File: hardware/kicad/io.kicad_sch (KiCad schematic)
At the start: 46 parts, among them J5 JST-XH 4p, J6 JST-XH 4p, J7 JST-XH 3p, J8 JST-XH 4p, J9 JST-XH 5p

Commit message: Add routed controller PCB, clutch CAD and mill notes
- Schematic: panel ribbon (2x7 IDC) + feed-unit header (JST-XH 7) so all
  connectors fit one 100 mm board edge; fix stub-bridging in the generator.
- PCB (hardware/tools/build_pcb.py): 100x100 mm 4-layer board built from the
  netlist - fixed placement for power/connectors, auto-placed passives,
  GND / split +36V/+3V3 inner planes, Freerouting, post-route power pours,
  GND stitching; fix_planes.py drops plane vias for leftovers;
  check_pcb.py runs DRC with schematic parity. 3D renders in hardware/renders.
  Status: 5 unconnected items + 2 starved thermals left for interactive
  routing (see hardware/kicad/drc.json after check_pcb.py).
- mechanical/clutch: parametric build123d model of the DIY tooth clutch
  (field housing, coil, rotor, armature, leaf springs, output hub/shaft,
  cover), STEP/STL export and VTK renders.
- docs/mill.md: SIEG X3.5D research and the measurements still needed.

Co-Authored-By: Claude Opus 5.5 <noreply@anthropic.com>
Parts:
- removed J6, J8: JST-XH 4p, Connector_JST:JST_XH_B4B-XH-A_1x04_P2.50mm_Vertical, symbol Connector_Generic:Conn_01x04
- removed J7: JST-XH 3p, Connector_JST:JST_XH_B3B-XH-A_1x03_P2.50mm_Vertical, symbol Connector_Generic:Conn_01x03
- removed J9: JST-XH 5p, Connector_JST:JST_XH_B5B-XH-A_1x05_P2.50mm_Vertical, symbol Connector_Generic:Conn_01x05
- added J4: PANEL 2x7 IDC, Connector_IDC:IDC-Header_2x07_P2.54mm_Vertical, symbol Connector_Generic:Conn_02x07_Odd_Even
- J5: value JST-XH 4p -> JST-XH 7p; footprint Connector_JST:JST_XH_B4B-XH-A_1x04_P2.50mm_Vertical -> Connector_JST:JST_XH_B7B-XH-A_1x07_P2.50mm_Vertical; symbol Connector_Generic:Conn_01x04 -> Connector_Generic:Conn_01x07; LCSC C144395 -> (none); MPN JST B4B-XH-A(LF)(SN) -> JST B7B-XH-A(LF)(SN)
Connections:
- net +3V3: now also J4.2 (Pin_2)
- net +5V: now also J5.1 (Pin_1)
- net DIAL_A_RAW: now also J4.11 (Pin_11)
- net DIAL_B_RAW: now also J4.12 (Pin_12)
- net DIAL_SW_RAW: now also J4.13 (Pin_13)
- net ENC_A_RAW: now also J5.3 (Pin_3)
- net ENC_B_RAW: now also J5.4 (Pin_4)
- net ENC_N_RAW: now also J5.5 (Pin_5)
- net ESTOP_RET: now also J4.7 (Pin_7)
- net GND: now also J5.2 (Pin_2), J4.1 (Pin_1), J4.14 (Pin_14), J4.5 (Pin_5); no longer J5.1 (Pin_1)
- net LIM_L_RAW: now also J5.6 (Pin_6)
- net LIM_R_RAW: now also J5.7 (Pin_7)
- net MODE_L_RAW: now also J4.8 (Pin_8); no longer J5.2 (Pin_2)
- net MODE_R_RAW: now also J4.9 (Pin_9); no longer J5.3 (Pin_3)
- net OLED_SCL: now also J4.3 (Pin_3)
- net OLED_SDA: now also J4.4 (Pin_4)
- net RAPID_RAW: now also J4.10 (Pin_10); no longer J5.4 (Pin_4)
- new net ESTOP_SRC: J4.6 (Pin_6)
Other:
- moved on the sheet: C36, C37, C38, C39, C40, C41, C42, C43, C44, C45, C46, D10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

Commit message: Complete LCSC part numbers in the BOM
Every BOM line now has an LCSC number except the Pico module (A1), which
is marked "user-supplied, hand-solder". Parts were checked against the
JLCPCB parts library for spec, Basic/Extended status and stock.

- build_schematic.py: RES_PARTS / CAP_PARTS value+footprint lookup tables
  used by R() / C(), which now raise if a passive has no entry; props for
  the diodes, LEDs, logic ICs, PTC (Littelfuse 2920L050DR, 60 V), IDC
  header (ZHOURI DC3-2.54-14PAS), JST-XH 7p and the Omron B3S-1000 reset
  button.
- Regenerated the schematic sheets, kicad/bom.csv, fab BOM and the README
  missing-LCSC table. PCB, CPL, gerbers and drills are unchanged.

Co-Authored-By: Claude Sonnet 5.5 <noreply@anthropic.com>
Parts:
- C36, C37, C38, C43: LCSC (none) -> C14663; MPN (none) -> Yageo CC0603KRX7R9BB104
- C39, C40, C41, C42: LCSC (none) -> C57112; MPN (none) -> FH 0603B103K500NT
- C44, C45, C46: LCSC (none) -> C14858; MPN (none) -> Samsung CL10C101JB8NNNC
- J4: LCSC (none) -> C2977595; MPN 2x7 2.54 mm shrouded box header -> ZHOURI DC3-2.54-14PAS (2x7 shrouded box header)
- J5: LCSC (none) -> C144398
- R48, R50, R52, R54, R56, R58, R60, R62, R70, R71: LCSC (none) -> C25804; MPN (none) -> UNI-ROYAL 0603WAF1002T5E
- R49, R51, R53, R55, R57, R59, R61, R63: LCSC (none) -> C21190; MPN (none) -> UNI-ROYAL 0603WAF1001T5E
- R64, R66, R68: LCSC (none) -> C4190; MPN (none) -> UNI-ROYAL 0603WAF2201T5E
- R65, R67, R69, R72, R73: LCSC (none) -> C22775; MPN (none) -> UNI-ROYAL 0603WAF1000T5E

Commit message: Schematic: bare RP2040 instead of the Pico module
RP2040 (QFN-56) per Raspberry Pi's minimal design: W25Q16JV 2 MB QSPI flash, 12 MHz crystal with 1k series,
internal 1.1 V core regulator, BOOTSEL + RESET buttons, JST-SH SWD, status LED on GPIO25, USB-C (5.1k CC,
27R series). +3V3 now from an AP2112K-3.3 fed by VSYS = +5V or USB VBUS through Schottkys. Same GPIO
numbers as the Pico, so the firmware is unchanged. ERC 0 findings, netlist 132 nets / 189 parts match.
Layout follows (PCB agent). LCSC numbers for the flash and crystal still to be verified.

Co-Authored-By: Claude Opus 5.5 <noreply@anthropic.com>
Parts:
- removed C36, C37, C38, C43: 100nF, Capacitor_SMD:C_0603_1608Metric, symbol Device:C
- removed C39, C40, C41, C42: 10nF, Capacitor_SMD:C_0603_1608Metric, symbol Device:C
- removed C44, C45, C46: 100pF, Capacitor_SMD:C_0603_1608Metric, symbol Device:C
- removed D10, D9: USBLC6-4SC6, Package_TO_SOT_SMD:SOT-23-6, symbol Power_Protection:USBLC6-4SC6
- removed J4: PANEL 2x7 IDC, Connector_IDC:IDC-Header_2x07_P2.54mm_Vertical, symbol Connector_Generic:Conn_02x07_Odd_Even
- removed J5: JST-XH 7p, Connector_JST:JST_XH_B7B-XH-A_1x07_P2.50mm_Vertical, symbol Connector_Generic:Conn_01x07
- removed R48, R50, R52, R54, R56: 10k, Resistor_SMD:R_0603_1608Metric, symbol Device:R
- removed R49, R51, R53, R55: 1k, Resistor_SMD:R_0603_1608Metric, symbol Device:R
- added C53, C54, C55, C60: 100nF, Capacitor_SMD:C_0603_1608Metric, symbol Device:C
- added C56, C57, C58, C59: 10nF, Capacitor_SMD:C_0603_1608Metric, symbol Device:C
- added C61, C62, C63: 100pF, Capacitor_SMD:C_0603_1608Metric, symbol Device:C
- added D13, D14: USBLC6-4SC6, Package_TO_SOT_SMD:SOT-23-6, symbol Power_Protection:USBLC6-4SC6
- added J6: PANEL 2x7 IDC, Connector_IDC:IDC-Header_2x07_P2.54mm_Vertical, symbol Connector_Generic:Conn_02x07_Odd_Even
- added J7: JST-XH 7p, Connector_JST:JST_XH_B7B-XH-A_1x07_P2.50mm_Vertical, symbol Connector_Generic:Conn_01x07
- added R74, R76, R78, R81, R82: 100, Resistor_SMD:R_0603_1608Metric, symbol Device:R
- added R75, R77: 2.2k, Resistor_SMD:R_0603_1608Metric, symbol Device:R
- added R79, R80: 10k, Resistor_SMD:R_0603_1608Metric, symbol Device:R
- R57, R59, R61, R63: value 1k -> 10k; LCSC C21190 -> C25804; MPN UNI-ROYAL 0603WAF1001T5E -> UNI-ROYAL 0603WAF1002T5E
- R58, R60, R62, R70: value 10k -> 1k; LCSC C25804 -> C21190; MPN UNI-ROYAL 0603WAF1002T5E -> UNI-ROYAL 0603WAF1001T5E
- R64, R66, R68: value 2.2k -> 1k; LCSC C4190 -> C21190; MPN UNI-ROYAL 0603WAF2201T5E -> UNI-ROYAL 0603WAF1001T5E
- R65, R67, R69: value 100 -> 10k; LCSC C22775 -> C25804; MPN UNI-ROYAL 0603WAF1000T5E -> UNI-ROYAL 0603WAF1002T5E
- R72: value 100 -> 1k; LCSC C22775 -> C21190; MPN UNI-ROYAL 0603WAF1000T5E -> UNI-ROYAL 0603WAF1001T5E
- R73: value 100 -> 2.2k; LCSC C22775 -> C4190; MPN UNI-ROYAL 0603WAF1000T5E -> UNI-ROYAL 0603WAF2201T5E
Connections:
- net +3V3: now also R57.1, R59.1, R61.1, R63.1, R65.1, R67.1, R69.1, R73.1, D13.5 (VBUS), D14.5 (VBUS), J6.2 (Pin_2), R75.1, R77.1, R79.1, R80.1; no longer R58.1, R60.1, R62.1, R64.1, R66.1, R68.1, R70.1
- net +5V: now also J7.1 (Pin_1)
- net DIAL_A: now also R68.2, C58.1; no longer R59.2
- net DIAL_A_RAW: now also D12.3 (I/O2), R67.2, R68.1, J6.11 (Pin_11); no longer R58.2, R59.1
- net DIAL_B: now also R70.2, C59.1; no longer R61.2
- net DIAL_B_RAW: now also D12.4 (I/O3), R69.2, R70.1, J6.12 (Pin_12); no longer R60.2, R61.1
- net DIAL_SW: now also R72.2, C60.1; no longer R63.2
- net DIAL_SW_RAW: now also D12.6 (I/O4), R71.2, R72.1, J6.13 (Pin_13); no longer R62.2, R63.1
- net ENC_A_RAW: now also R73.2, D13.1 (I/O1), J7.3 (Pin_3), R74.1; no longer D11.1 (I/O1), R64.2, R65.1
- net ENC_B_RAW: now also D13.3 (I/O2), J7.4 (Pin_4), R75.2, R76.1; no longer D11.3 (I/O2), R66.2, R67.1
- net ENC_N_RAW: now also D13.4 (I/O3), J7.5 (Pin_5), R77.2, R78.1; no longer D11.4 (I/O3), R68.2, R69.1
- net ENC_OUT_A: now also C61.1, R74.2; no longer R65.2
- net ENC_OUT_B: now also C62.1, R76.2; no longer R67.2
- net ENC_OUT_N: now also C63.1, R78.2; no longer R69.2
- net ESTOP_RET: now also D13.6 (I/O4), J6.7 (Pin_7); no longer D11.6 (I/O4)
- net ESTOP_SRC: now also J6.6 (Pin_6)
- net GND: now also C53.2, C54.2, C55.2, C56.2, C57.2, C58.2, C59.2, C60.2, C61.2, C62.2, C63.2, D13.2 (GND), D14.2 (GND), J6.1 (Pin_1), J6.14 (Pin_14), J6.5 (Pin_5), J7.2 (Pin_2)
- net I2C_SCL: now also R81.2; no longer R72.2
- net I2C_SDA: now also R82.2; no longer R73.2
- net LIM_L: now also R64.2, C56.1
- net LIM_L_RAW: now also D11.6 (I/O4), R63.2, R64.1, J7.6 (Pin_6)
- net LIM_R: now also R66.2, C57.1; no longer R57.2
- net LIM_R_RAW: now also D12.1 (I/O1), R65.2, R66.1, J7.7 (Pin_7); no longer R57.1
- net MODE_L: now also R58.2, C53.1
- net MODE_L_RAW: now also D11.1 (I/O1), R57.2, R58.1, J6.8 (Pin_8)
- net MODE_R: now also R60.2, C54.1
- net MODE_R_RAW: now also D11.3 (I/O2), R59.2, R60.1, J6.9 (Pin_9)
- net OLED_SCL: now also D14.1 (I/O1), J6.3 (Pin_3), R79.2, R81.1; no longer D12.1 (I/O1), R70.2, R72.1
- net OLED_SDA: now also D14.3 (I/O2), J6.4 (Pin_4), R80.2, R82.1; no longer D12.3 (I/O2), R71.2, R73.1
- net RAPID: now also R62.2, C55.1
- net RAPID_RAW: now also D11.4 (I/O3), R61.2, R62.1, J6.10 (Pin_10)
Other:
- note added: "All panel inputs: pull-up at the connector, ESD array, series R + RC filter into the logic. Switch contacts go to GND (active low). Limit switches are NC to GND, so a broken wire reads as 'hit'. Output encoder (LPD3806, NPN open collector) powered from 5 V, pulled up to 3.3 V (safe for the RP2040 + TMC5160)."
- note removed: "All panel inputs: pull-up at the connector, ESD array, series R + RC filter into the logic. Switch contacts go to GND (active low). Limit switches are NC to GND, so a broken wire reads as 'hit'. Output encoder (LPD3806, NPN open collector) powered from 5 V, pulled up to 3.3 V (safe for Pico + TMC5160)."
- moved on the sheet: D11, D12, R57, R58, R59, R60, R61, R62, R63, R64, R65, R66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

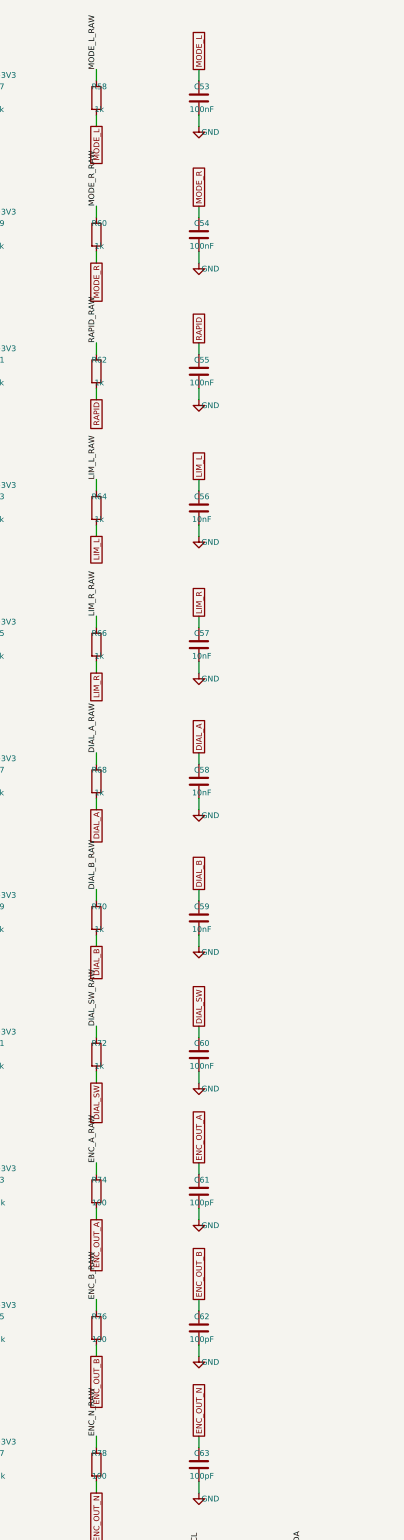
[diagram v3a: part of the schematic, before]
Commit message: Schematic: 100 nF right at RP2040 DVDD pin 23 and USBLC6-2SC6 ESD (C7519) on the USB-C lines (PCB review round 2)
Co-Authored-By: Claude Opus 5.5 <noreply@anthropic.com>
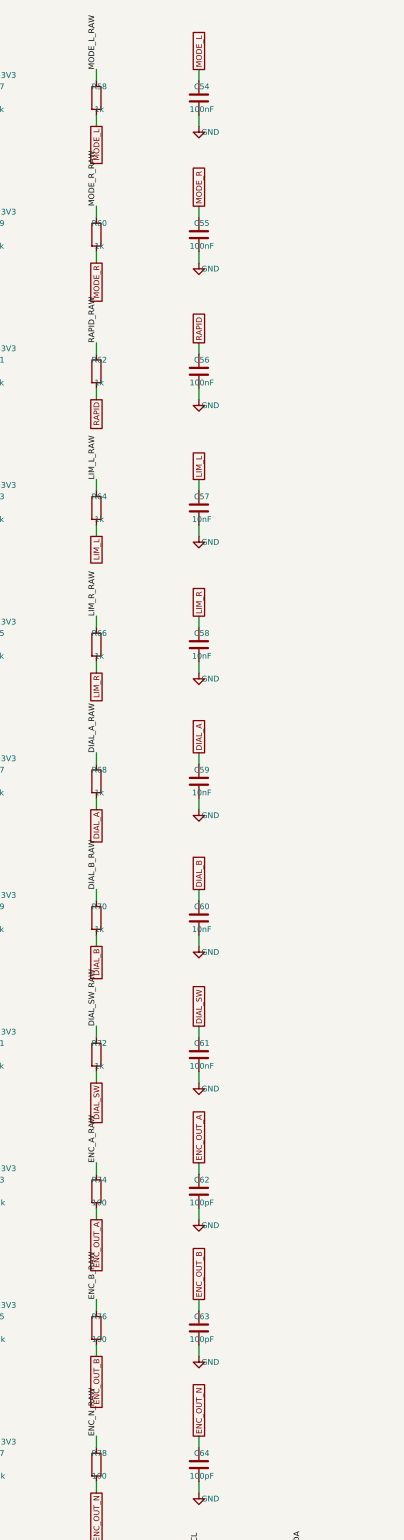
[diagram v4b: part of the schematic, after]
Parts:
- removed C53: 100nF, Capacitor_SMD:C_0603_1608Metric, symbol Device:C
- added C64: 100pF, Capacitor_SMD:C_0603_1608Metric, symbol Device:C
- C56: value 10nF -> 100nF; LCSC C57112 -> C14663; MPN FH 0603B103K500NT -> Yageo CC0603KRX7R9BB104
- C60: value 100nF -> 10nF; LCSC C14663 -> C57112; MPN Yageo CC0603KRX7R9BB104 -> FH 0603B103K500NT
- C61: value 100pF -> 100nF; LCSC C14858 -> C14663; MPN Samsung CL10C101JB8NNNC -> Yageo CC0603KRX7R9BB104
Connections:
- net DIAL_A: now also C59.1; no longer C58.1
- net DIAL_B: now also C60.1; no longer C59.1
- net DIAL_SW: now also C61.1; no longer C60.1
- net ENC_OUT_A: now also C62.1; no longer C61.1
- net ENC_OUT_B: now also C63.1; no longer C62.1
- net ENC_OUT_N: now also C64.1; no longer C63.1
- net GND: now also C64.2
- net LIM_L: now also C57.1; no longer C56.1
- net LIM_R: now also C58.1; no longer C57.1
- net MODE_L: now also C54.1
- net MODE_R: now also C55.1; no longer C54.1
- net RAPID: now also C56.1; no longer C55.1
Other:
- moved on the sheet: C54, C55, C56, C57, C58, C59, C60, C61, C62, C63
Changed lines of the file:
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@@
 		(on_board yes)
 		(dnp no)
-		(property "Reference" "C53"
+		(property "Reference" "C54"
 			(at 76.835 96.52 0)
 			(effects
@@
 			(project "power-feed"
 				(path "/8e300617-3fca-5828-bedd-07eaa661f340/302f738b-0c7f-5b37-9d65-0eee6b5d5df7"
-					(reference "C53")
+					(reference "C54")
 					(unit 1)
 				)
@@
 		(on_board yes)
 		(dnp no)
-		(property "Reference" "C54"
+		(property "Reference" "C55"
 			(at 76.835 127 0)
 			(effects
@@
 			(project "power-feed"
 				(path "/8e300617-3fca-5828-bedd-07eaa661f340/302f738b-0c7f-5b37-9d65-0eee6b5d5df7"
-					(reference "C54")
+					(reference "C55")
 					(unit 1)
 				)
@@
 		(on_board yes)
 		(dnp no)
-		(property "Reference" "C55"
+		(property "Reference" "C56"
 			(at 76.835 157.48 0)
 			(effects
@@
 			(project "power-feed"
 				(path "/8e300617-3fca-5828-bedd-07eaa661f340/302f738b-0c7f-5b37-9d65-0eee6b5d5df7"
-					(reference "C55")
+					(reference "C56")
 					(unit 1)
 				)
@@
 		(on_board yes)
 		(dnp no)
-		(property "Reference" "C56"
+		(property "Reference" "C57"
 			(at 76.835 187.96 0)
 			(effects
@@
 			(project "power-feed"
 				(path "/8e300617-3fca-5828-bedd-07eaa661f340/302f738b-0c7f-5b37-9d65-0eee6b5d5df7"
-					(reference "C56")
+					(reference "C57")
 					(unit 1)
 				)
@@
 		(on_board yes)
 		(dnp no)
-		(property "Reference" "C57"
+		(property "Reference" "C58"
 			(at 76.835 218.44 0)
 			(effects
@@
 			(project "power-feed"
 				(path "/8e300617-3fca-5828-bedd-07eaa661f340/302f738b-0c7f-5b37-9d65-0eee6b5d5df7"
-					(reference "C57")
+					(reference "C58")
 					(unit 1)
 				)
@@
 		(on_board yes)
 		(dnp no)
-		(property "Reference" "C58"
+		(property "Reference" "C59"
 			(at 76.835 248.92 0)
 			(effects
@@
 			(project "power-feed"
 				(path "/8e300617-3fca-5828-bedd-07eaa661f340/302f738b-0c7f-5b37-9d65-0eee6b5d5df7"
-					(reference "C58")
+					(reference "C59")
 					(unit 1)
 				)
@@
 		(on_board yes)
 		(dnp no)
-		(property "Reference" "C59"
+		(property "Reference" "C60"
 			(at 76.835 279.4 0)
 			(effects
@@
 			(project "power-feed"
 				(path "/8e300617-3fca-5828-bedd-07eaa661f340/302f738b-0c7f-5b37-9d65-0eee6b5d5df7"
-					(reference "C59")
+					(reference "C60")
 					(unit 1)
 				)
@@
 		(on_board yes)
 		(dnp no)
-		(property "Reference" "C60"
+		(property "Reference" "C61"
 			(at 76.835 309.88 0)
 			(effects
@@
 			(project "power-feed"
 				(path "/8e300617-3fca-5828-bedd-07eaa661f340/302f738b-0c7f-5b37-9d65-0eee6b5d5df7"
-					(reference "C60")
+					(reference "C61")
 					(unit 1)
 				)
@@
 		(on_board yes)
 		(dnp no)
-		(property "Reference" "C61"
+		(property "Reference" "C62"
 			(at 76.835 340.36 0)
 			(effects
@@
 			(project "power-feed"
 				(path "/8e300617-3fca-5828-bedd-07eaa661f340/302f738b-0c7f-5b37-9d65-0eee6b5d5df7"
-					(reference "C61")
+					(reference "C62")
 					(unit 1)
 				)
@@
 		(on_board yes)
 		(dnp no)
-		(property "Reference" "C62"
+		(property "Reference" "C63"
 			(at 76.835 370.84 0)
 			(effects
@@
 			(project "power-feed"
 				(path "/8e300617-3fca-5828-bedd-07eaa661f340/302f738b-0c7f-5b37-9d65-0eee6b5d5df7"
-					(reference "C62")
+					(reference "C63")
 					(unit 1)
 				)
@@
 		(on_board yes)
 		(dnp no)
-		(property "Reference" "C63"
+		(property "Reference" "C64"
 			(at 76.835 401.32 0)
 			(effects
@@
 			(project "power-feed"
 				(path "/8e300617-3fca-5828-bedd-07eaa661f340/302f738b-0c7f-5b37-9d65-0eee6b5d5df7"
-					(reference "C63")
+					(reference "C64")
 					(unit 1)
 				)
